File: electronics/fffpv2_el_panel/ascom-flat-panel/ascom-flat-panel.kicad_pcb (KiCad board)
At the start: 2 copper layers, 56 x 32 mm, 14 parts, among them J1 Servo, J2 JST-XH LED, Q1 IRLZ34N, Q2 IRLZ34N, U1 XIAO-SAMD21-DIP

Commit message: [electronics] - intialisation PCB v2. Gros travail de routage en perspective :D
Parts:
- removed the G*** at (120.5, 96.0)
- removed J2: JST-XH LED, Connector_JST:JST_XH_B2B-XH-A_1x02_P2.50mm_Vertical
- added C2: 22nF, Capacitor_THT:C_Disc_D3.0mm_W1.6mm_P2.50mm, F.Cu at (143.8, 91.5)
- added C3: 10µF, Capacitor_THT:C_Radial_D6.3mm_H11.0mm_P2.50mm, F.Cu at (100.6, 106.5)
- added R5: 1M, Resistor_THT:R_Axial_DIN0207_L6.3mm_D2.5mm_P10.16mm_Horizontal, F.Cu at (139.7, 91.5)
- added Rf1: 82k, Resistor_THT:R_Axial_DIN0207_L6.3mm_D2.5mm_P10.16mm_Horizontal, F.Cu at (122.8, 117.8)
- added Rin1: 38kΩ, Resistor_THT:R_Axial_DIN0207_L6.3mm_D2.5mm_P10.16mm_Horizontal, F.Cu at (148.2, 104.9)
- added U2: TLC272, Package_DIP:DIP-8_W7.62mm, F.Cu at (130.9, 123.1)
- added U3: ~, CustomFootprints:DFR052 DC regulator, F.Cu at (116.4, 108.1)
- moved Q2 11.6 mm to (142.0, 108.6)
- moved R4 8.91 mm to (127.9, 97.1)
- moved R3 8.74 mm to (117.8, 93.2)
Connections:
- Q2 pad 2: Net-(J2-Pin_2) -> EL PANEL CONTROL CIRCUIT
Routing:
- net LED_STRIP_POWER_CONTROL: track 14.5 -> 0.00 mm
- net Net-(Q2-G): track 11.7 -> 0.00 mm
- net Net-(J2-Pin_2): track 11.6 -> 0.00 mm
- net +5V: track 41.2 -> 30.0 mm
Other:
- board size 56 x 32 mm -> 56 x 55 mm
- board text removed: "LED"

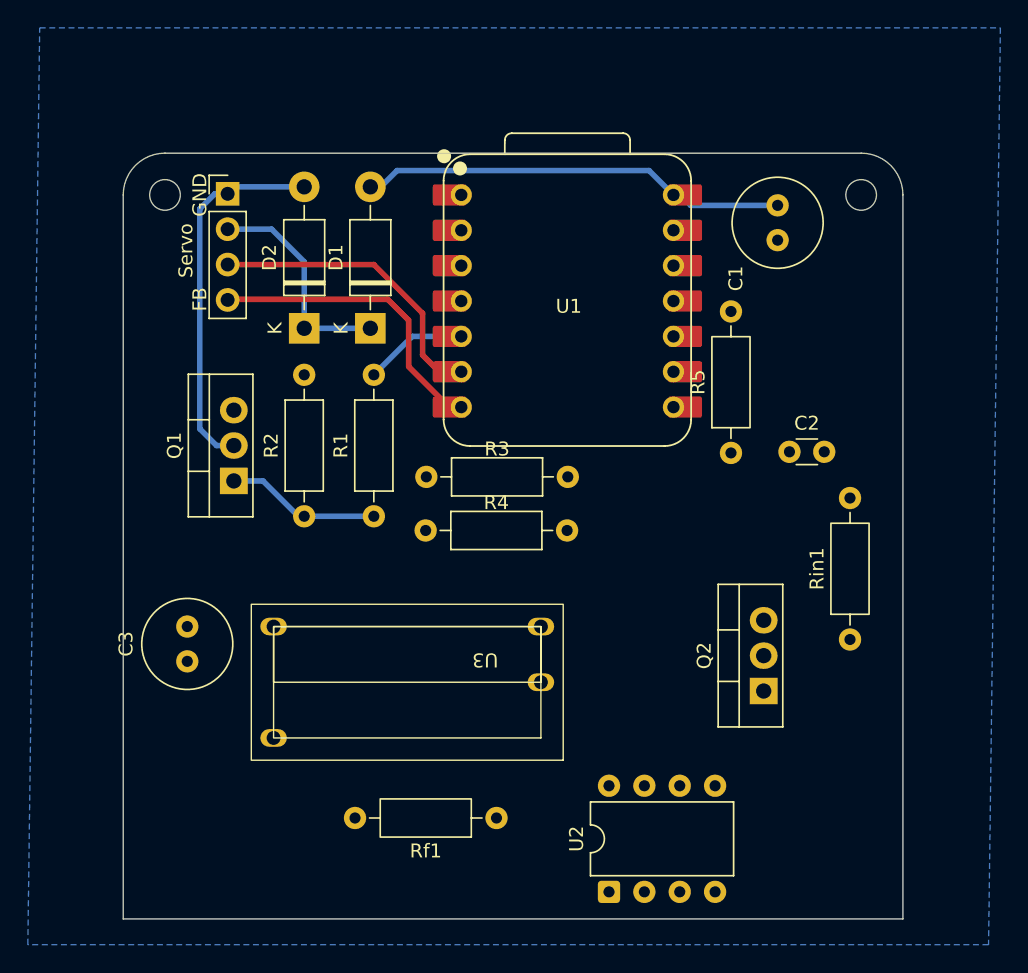
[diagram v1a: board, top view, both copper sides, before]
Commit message: First PCB routing
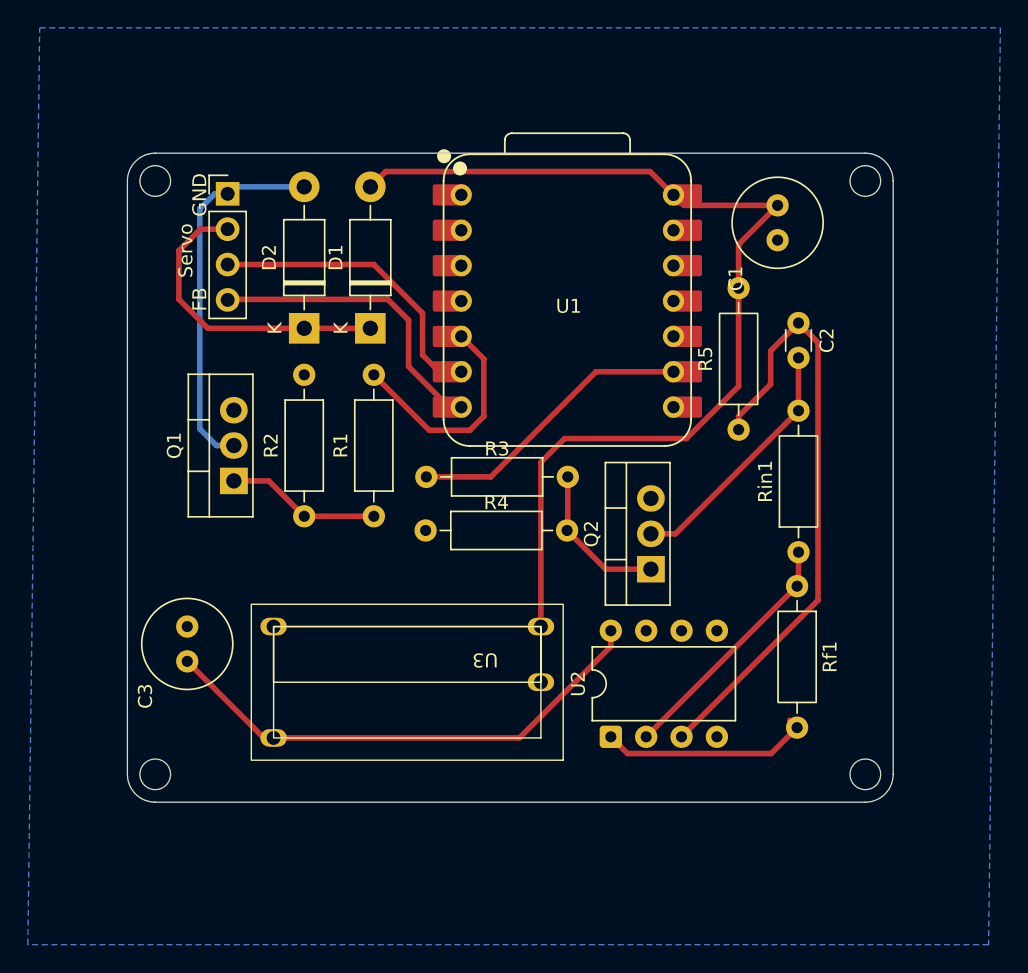
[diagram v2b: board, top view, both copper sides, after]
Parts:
- moved Rf1 27.3 mm to (144.4, 101.1), turned to -90 degrees
- moved Q2 11.9 mm to (133.9, 99.9)
- moved U2 11.1 mm to (131.0, 111.9)
- moved C2 9.27 mm to (144.5, 82.2), turned to -90 degrees
- moved Rin1 7.28 mm to (144.5, 98.7)
- moved R5 1.76 mm to (140.2, 89.9)
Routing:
- net +5V: track 30.0 -> 74.7 mm
- net Net-(U2A-+): track 0.00 -> 44.0 mm
- net +12V: track 0.00 -> 36.6 mm
- net LED_STRIP_POWER_CONTROL: track 0.00 -> 20.9 mm
- net EL PANEL CONTROL CIRCUIT: track 0.00 -> 18.1 mm
- net Net-(U2A--): track 0.00 -> 18.0 mm
- net EL_DRIVER+: track 0.00 -> 15.4 mm
- net Net-(Q2-G): track 0.00 -> 11.0 mm
- net SERVO POWER CONTROL: track 7.42 -> 16.4 mm
- net SERVO VCC: track 15.5 -> 22.2 mm
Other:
- board size 56 x 55 mm -> 55 x 46.6 mm

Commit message: Adding power planes to simplify PCB layout
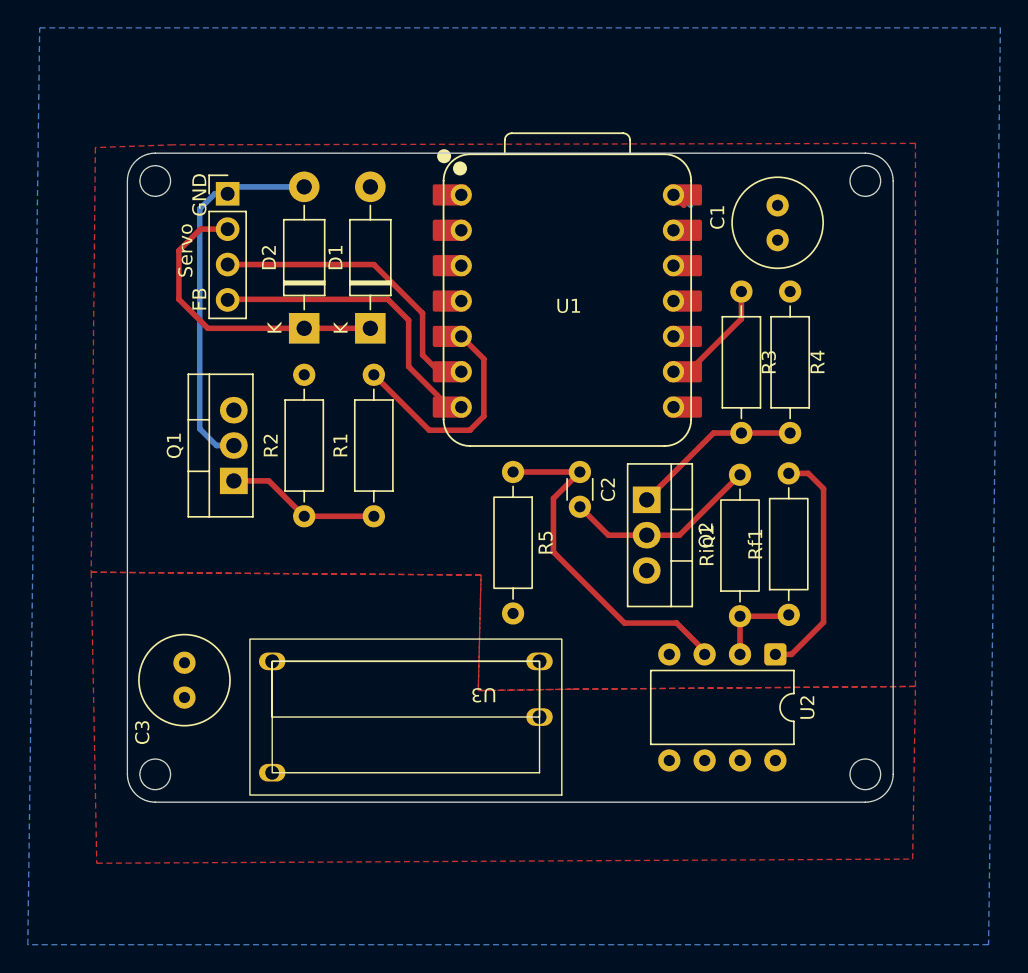
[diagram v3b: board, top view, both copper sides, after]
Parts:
- moved R3 26.3 mm to (140.4, 79.9), turned to -90 degrees
- moved C2 19.0 mm to (128.8, 92.9)
- moved R4 17.5 mm to (143.9, 90.1), turned to 90 degrees
- moved R5 16.5 mm to (124.0, 92.9), turned to -90 degrees
- moved U2 13.2 mm to (142.8, 106.0), turned to -90 degrees
- moved Rin1 6.23 mm to (140.3, 103.3)
- moved Q2 4.99 mm to (133.6, 94.9), turned to -90 degrees
- moved C3 2.61 mm to (100.4, 109.1)
- moved U3 2.50 mm to (116.3, 110.6)
- moved Rf1 2.15 mm to (143.8, 103.2), turned to 90 degrees
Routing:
- net +5V: track 74.7 -> 2.60 mm
- net +12V: track 36.6 -> 0.00 mm
- net Net-(U2A-+): track 44.0 -> 25.4 mm
- net LED_STRIP_POWER_CONTROL: track 20.9 -> 8.41 mm
- net Net-(U2A--): track 18.0 -> 6.28 mm
- net EL PANEL CONTROL CIRCUIT: track 18.1 -> 14.1 mm
- net EL_DRIVER+: track 15.4 -> 17.0 mm
- net Net-(Q2-G): track 11.0 -> 12.3 mm
- added copper zone on F.Cu, net +12V
- added copper zone on F.Cu, net +5V
